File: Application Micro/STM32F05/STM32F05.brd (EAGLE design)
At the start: 100 x 80 mm, 43 parts, among them T1 FDN340P

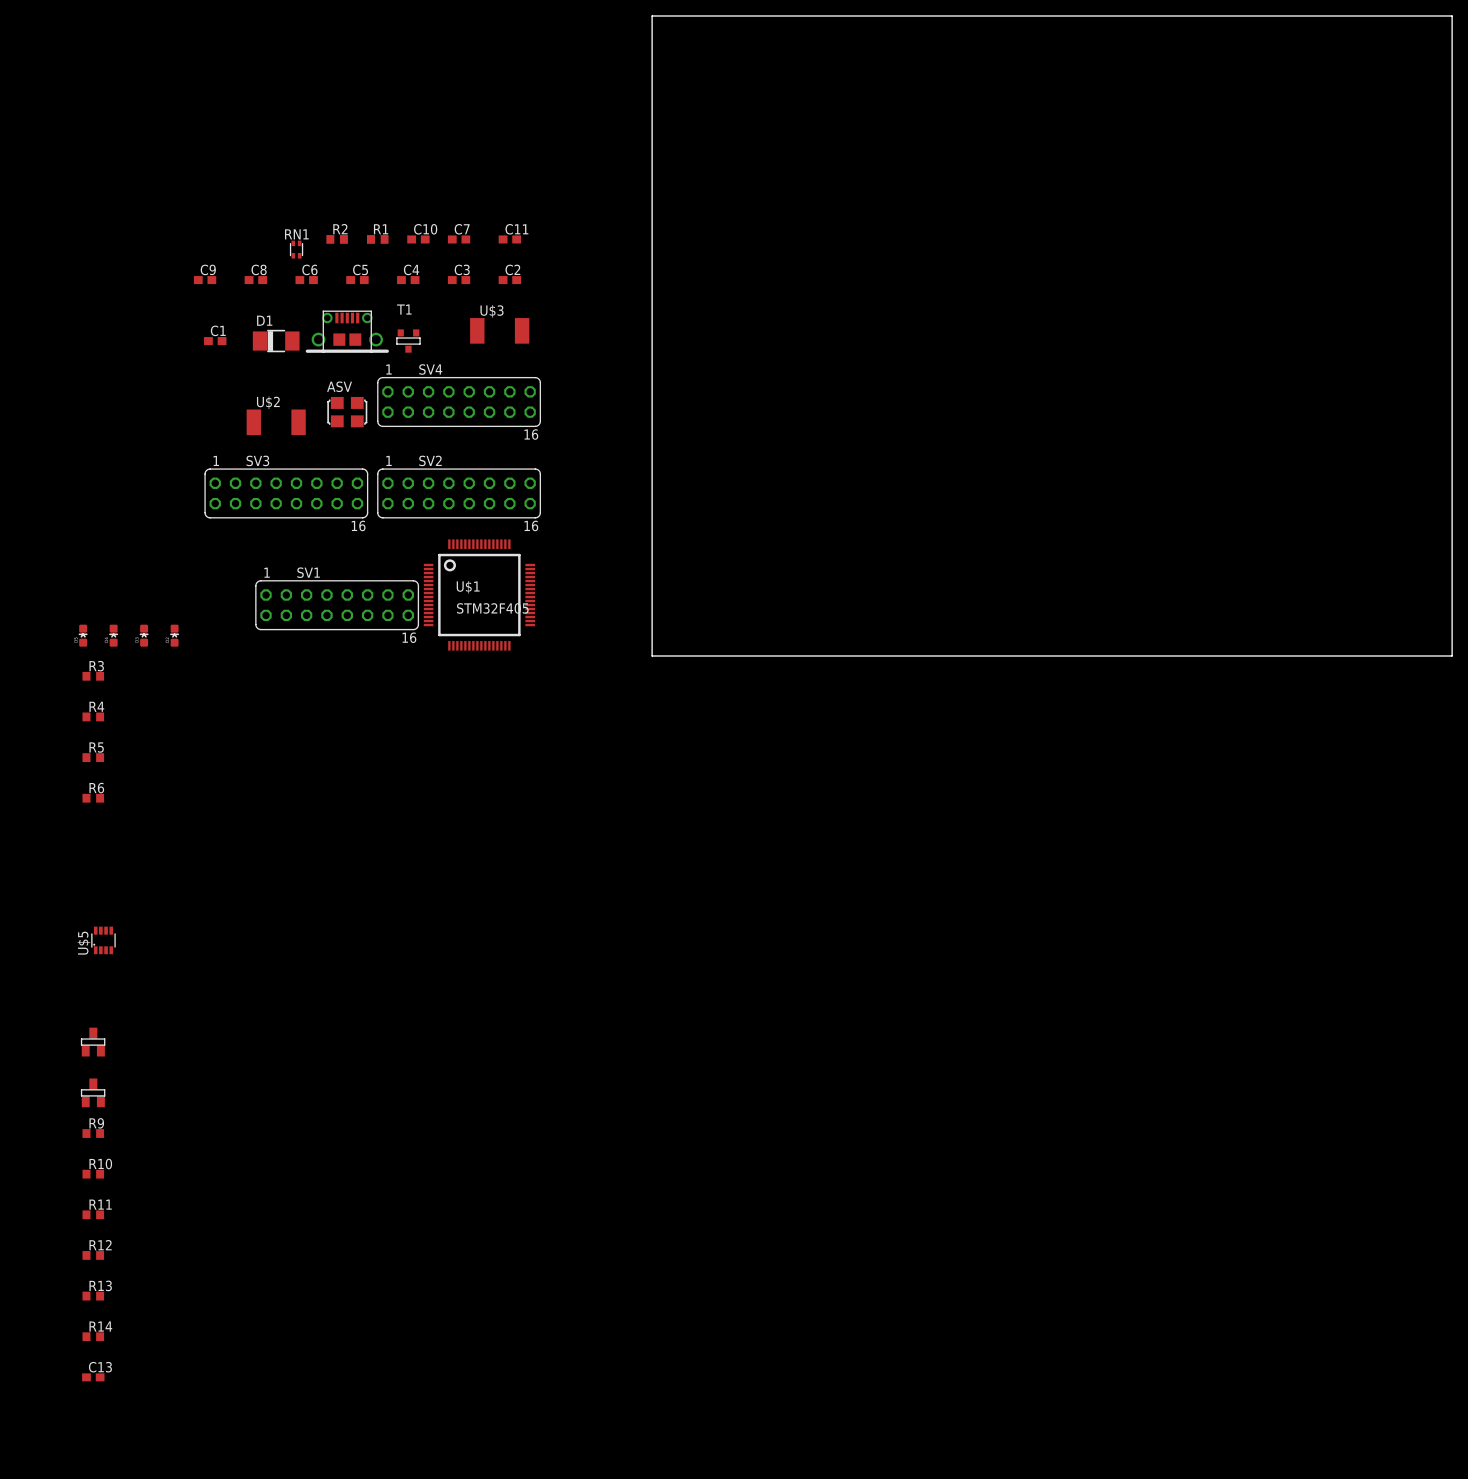
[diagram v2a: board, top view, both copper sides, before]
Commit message: Added last parts to application board microcontroller.
Added the linear regulator, finished as much of schematic as we can for
now. *I think*  Now all that's left is deciding what pins do what.
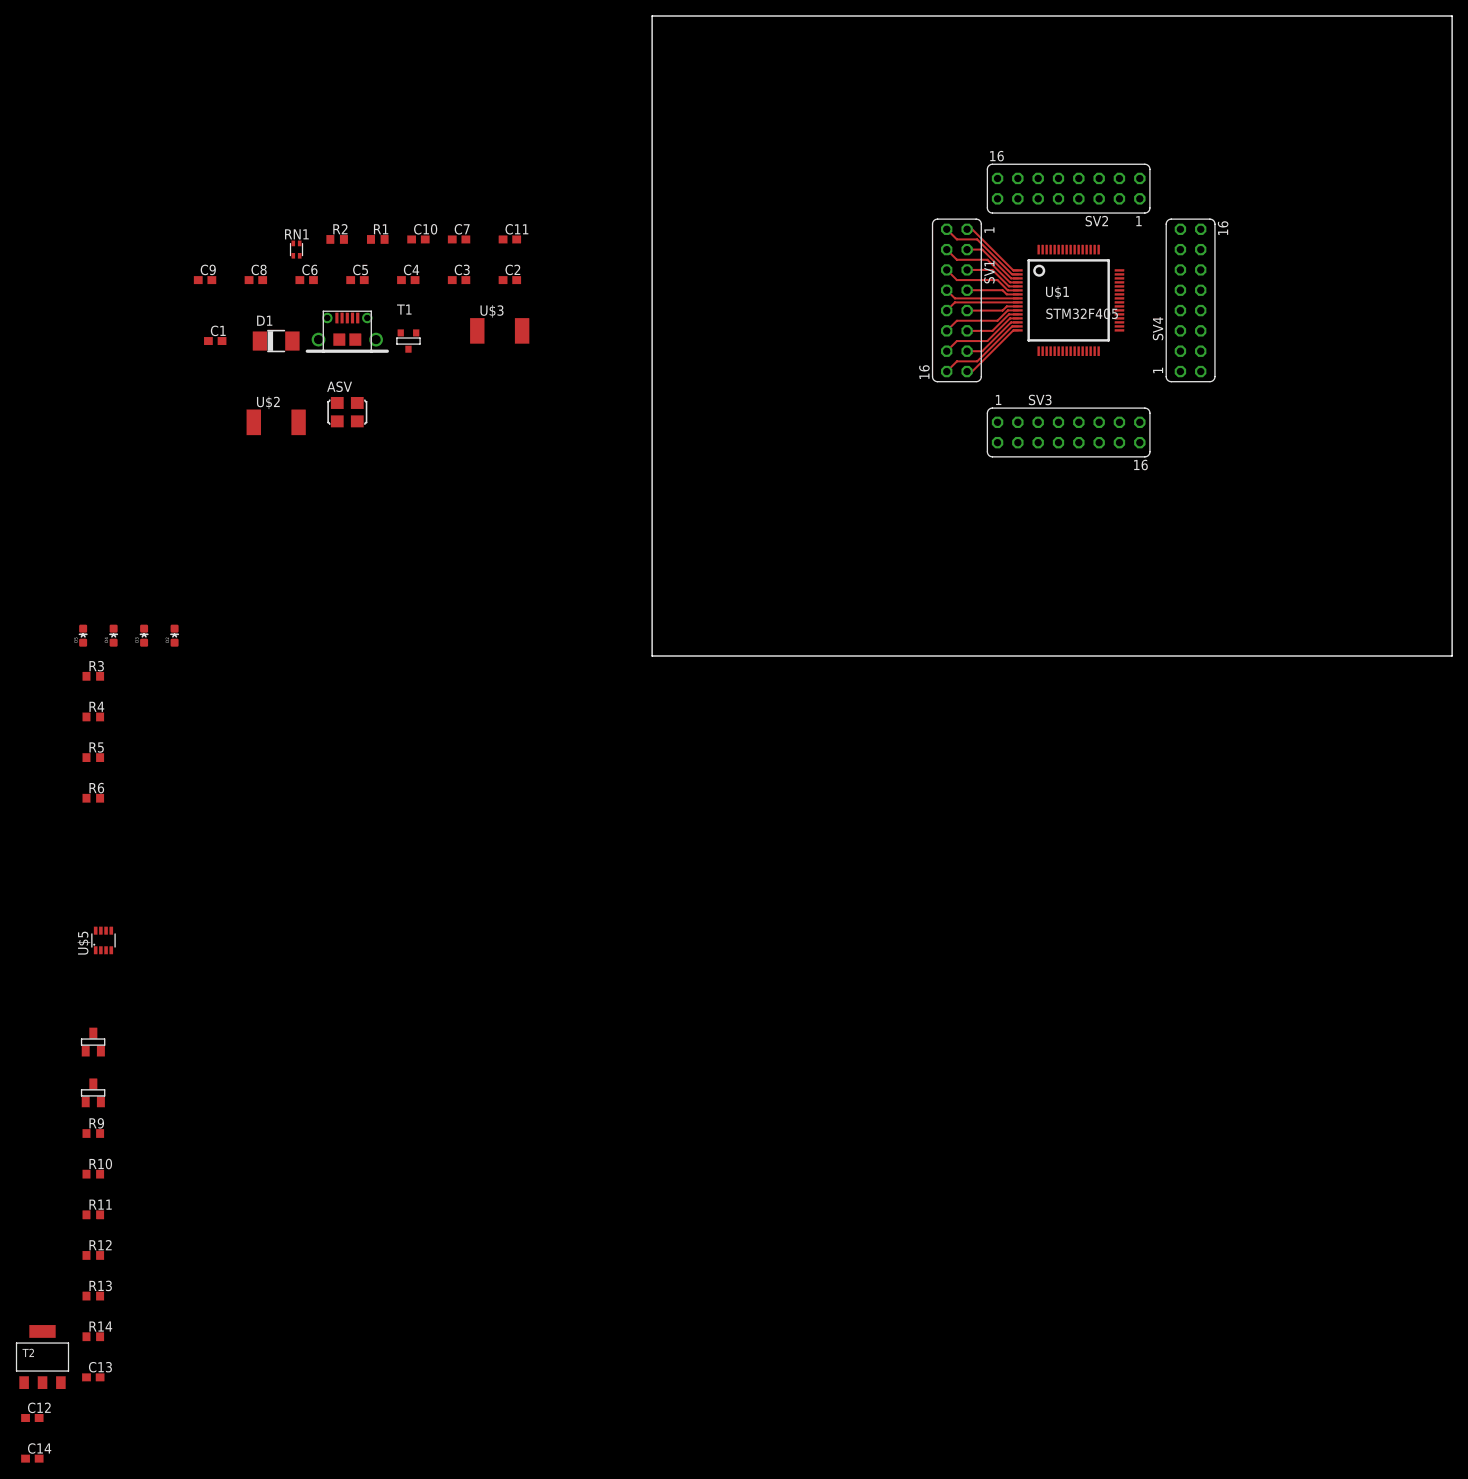
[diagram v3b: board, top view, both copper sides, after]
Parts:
- added C12, C14: 0.22uF, rcl:C0603
- added T2: AP1117_LIN_REG, PowerComponents:SOT223
- moved SV3 98.1 mm to (52.1, 27.9)
- moved SV4 92.3 mm to (67.3, 44.5), turned to 90 degrees
- moved SV1 86.3 mm to (38.1, 44.5), turned to 270 degrees
- moved SV2 85.2 mm to (52.1, 58.4), turned to 180 degrees
- moved U$1 82.4 mm to (52.1, 44.5)
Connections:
- new net USBD+: RN1.3
- new net USBD-: RN1.4
- net +3V3: now also C14.1, SV1.14, T2.TAB, T2.VOUT; no longer SV1.13
- net GND: now also C12.2, C14.2, SV1.11, T2.GND; no longer SV1.12
- net N$58: now also C12.1, T2.VIN
- net PIN10: now also SV1.9; no longer SV1.10
- net PIN11: now also SV1.12; no longer SV1.11
- net PIN14: now also SV1.13; no longer SV1.14
- net PIN15: now also SV1.16; no longer SV1.15
- net PIN16: now also SV1.15; no longer SV1.16
- net PIN9: now also SV1.10; no longer SV1.9
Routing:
- net +3V3: track 0.00 -> 19.1 mm
- net PIN2: track 0.00 -> 11.2 mm
- net PIN15: track 0.00 -> 11.2 mm
- net PIN4: track 0.00 -> 10.6 mm
- net PIN11: track 0.00 -> 9.95 mm
- net OSCOUT: track 0.00 -> 9.95 mm
- net PIN9: track 0.00 -> 9.31 mm
- net PIN8: track 0.00 -> 9.31 mm
- net PIN16: track 0.00 -> 7.84 mm
- net PIN14: track 0.00 -> 7.84 mm
- net PIN3: track 0.00 -> 7.84 mm
- net GND: track 0.00 -> 7.20 mm
- net OSCIN: track 0.00 -> 7.20 mm
- net PIN10: track 0.00 -> 6.57 mm
- net NRST: track 0.00 -> 6.57 mm

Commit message: Connected the programming pins
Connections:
- net PIN44: no longer U$1.44
- net PIN45: no longer U$1.45
- net USBD+: now also U$1.45
- net USBD-: now also U$1.44
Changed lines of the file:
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@@
 </signal>
 <signal name="PIN44">
-<contactref element="U$1" pad="44"/>
 <contactref element="SV4" pad="12"/>
-<wire x1="58.42" y1="46.2" x2="68.58" y2="48.26" width="0" layer="19" extent="1-1"/>
 </signal>
 <signal name="PIN45">
-<contactref element="U$1" pad="45"/>
 <contactref element="SV4" pad="13"/>
-<wire x1="58.42" y1="46.7" x2="66.04" y2="50.8" width="0" layer="19" extent="1-1"/>
 </signal>
 <signal name="PIN46">
@@
 <signal name="USBD-">
 <contactref element="RN1" pad="4"/>
+<contactref element="U$1" pad="44"/>
+<wire x1="-44.85" y1="51.575" x2="58.42" y2="46.2" width="0" layer="19" extent="1-1"/>
 </signal>
 <signal name="USBD+">
 <contactref element="RN1" pad="3"/>
+<contactref element="U$1" pad="45"/>
+<wire x1="-44.05" y1="51.575" x2="58.42" y2="46.7" width="0" layer="19" extent="1-1"/>
 </signal>
 </signals>
